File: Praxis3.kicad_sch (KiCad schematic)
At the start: 44 parts, among them IC60 HCF4094YM013TR, IC61 HCF4094YM013TR, Q66 2N7002, Q67 2N7002, Q68 2N7002, Q69 2N7002, Q70 2N7002, Q71 2N7002, Q72 2N7002, SW60 MSS6-V-T_R, SW61 B3U-3100P, SW62 B3U-3100P

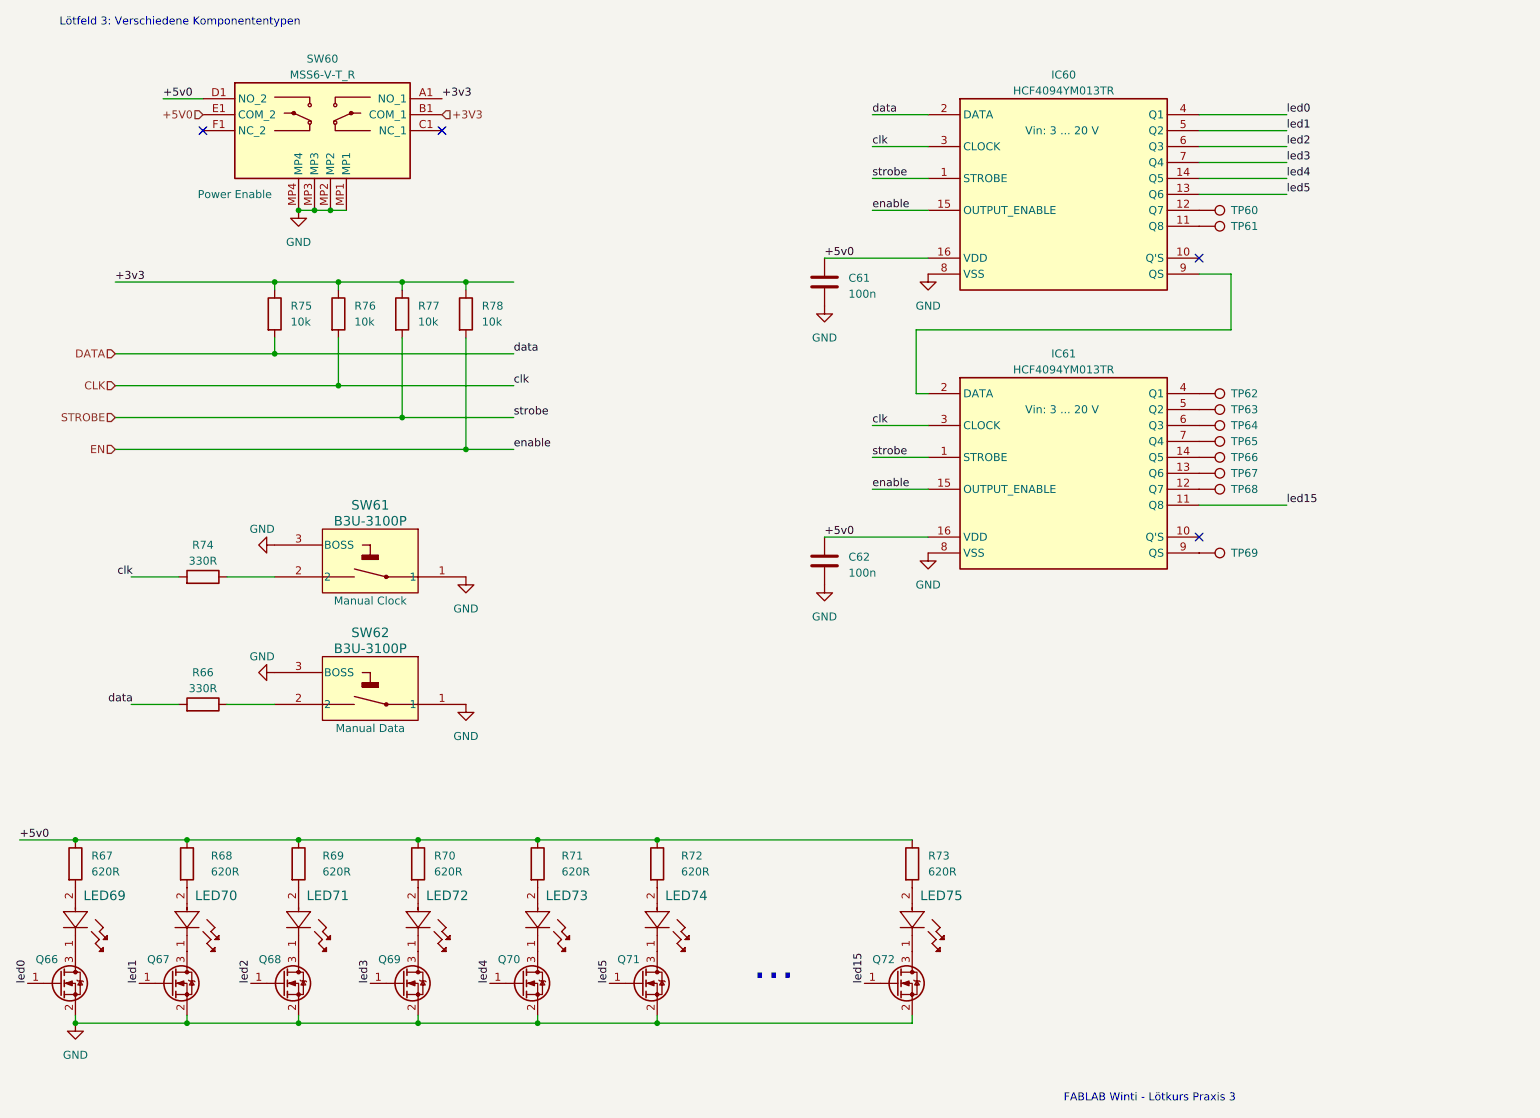
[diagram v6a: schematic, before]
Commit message: Added C for all digital signals
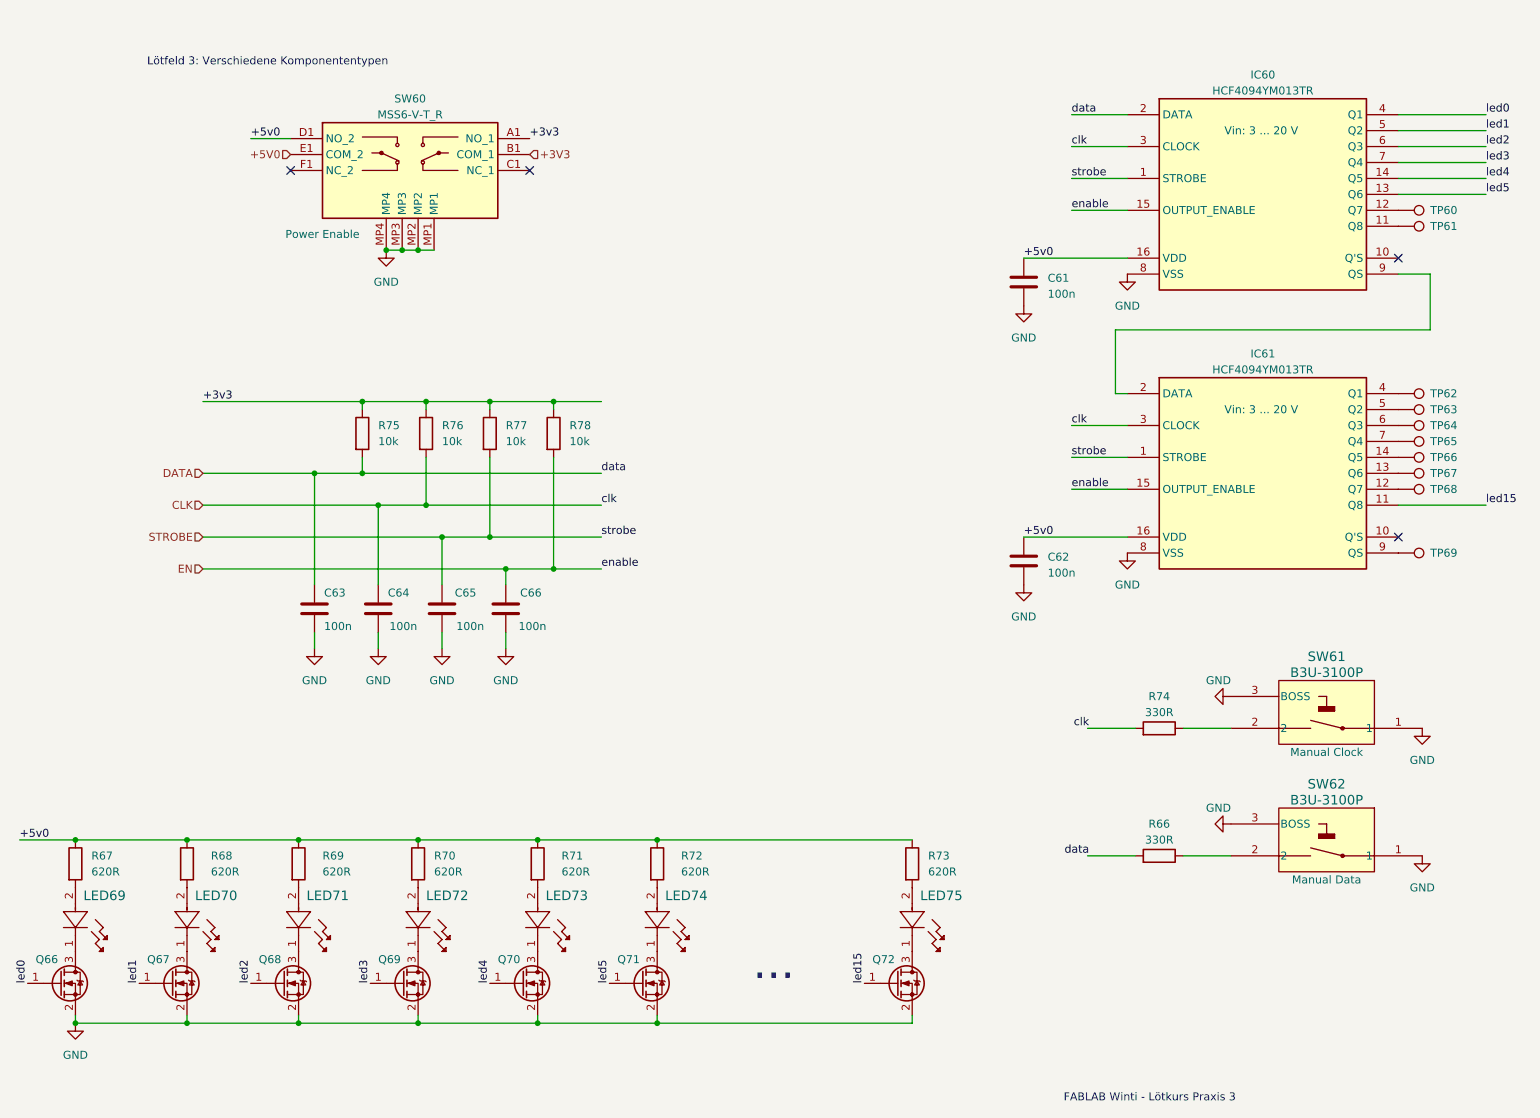
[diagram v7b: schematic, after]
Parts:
- added C63, C64, C65, C66: 100n, Capacitor_SMD:C_1206_3216Metric, symbol Device:C
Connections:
- net CLK: now also C64.1
- net DATA: now also C63.1
- net EN: now also C66.1
- net GND: now also C63.2, C64.2, C65.2, C66.2
- net STROBE: now also C65.1
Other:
- moved on the sheet: C61, C62, IC60, IC61, R66, R74, R75, R76, R77, R78, SW60, SW61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
